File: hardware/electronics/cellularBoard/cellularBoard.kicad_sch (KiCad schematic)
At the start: 36 parts, among them J1 Standoff, J2 M.2_E_Key_PCB_Edge, U1 LM51571-Q1

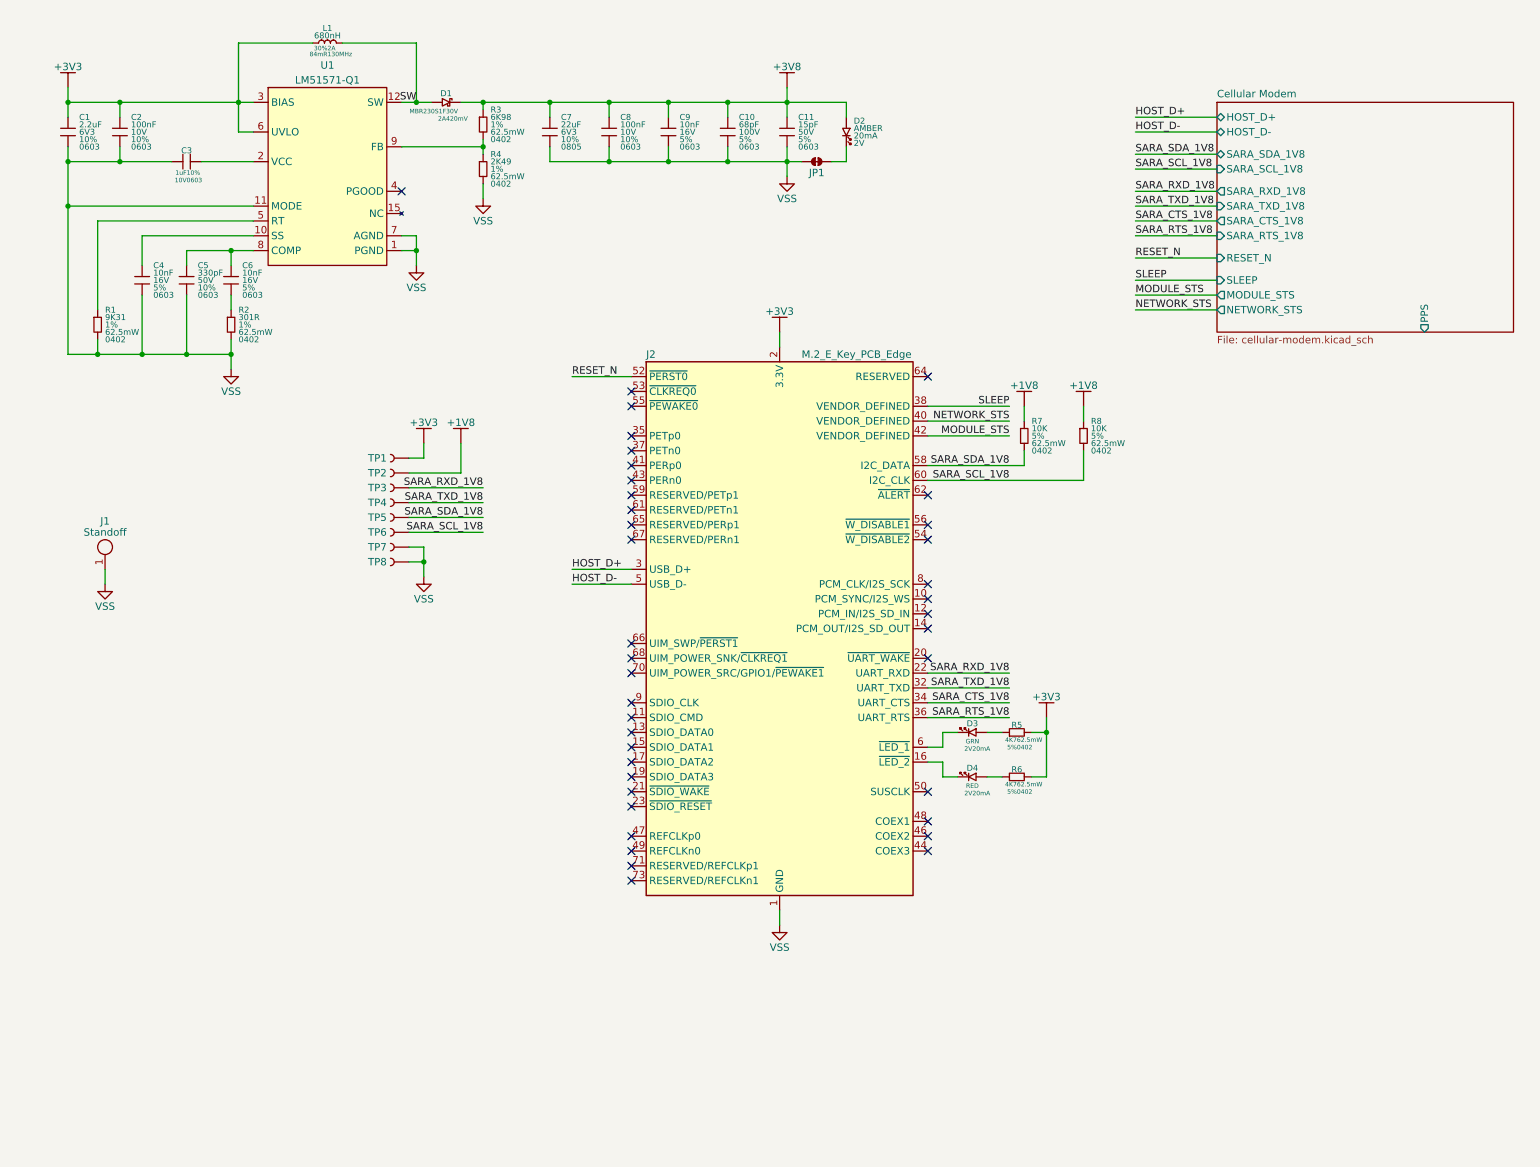
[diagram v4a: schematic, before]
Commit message: cleaned up schematic
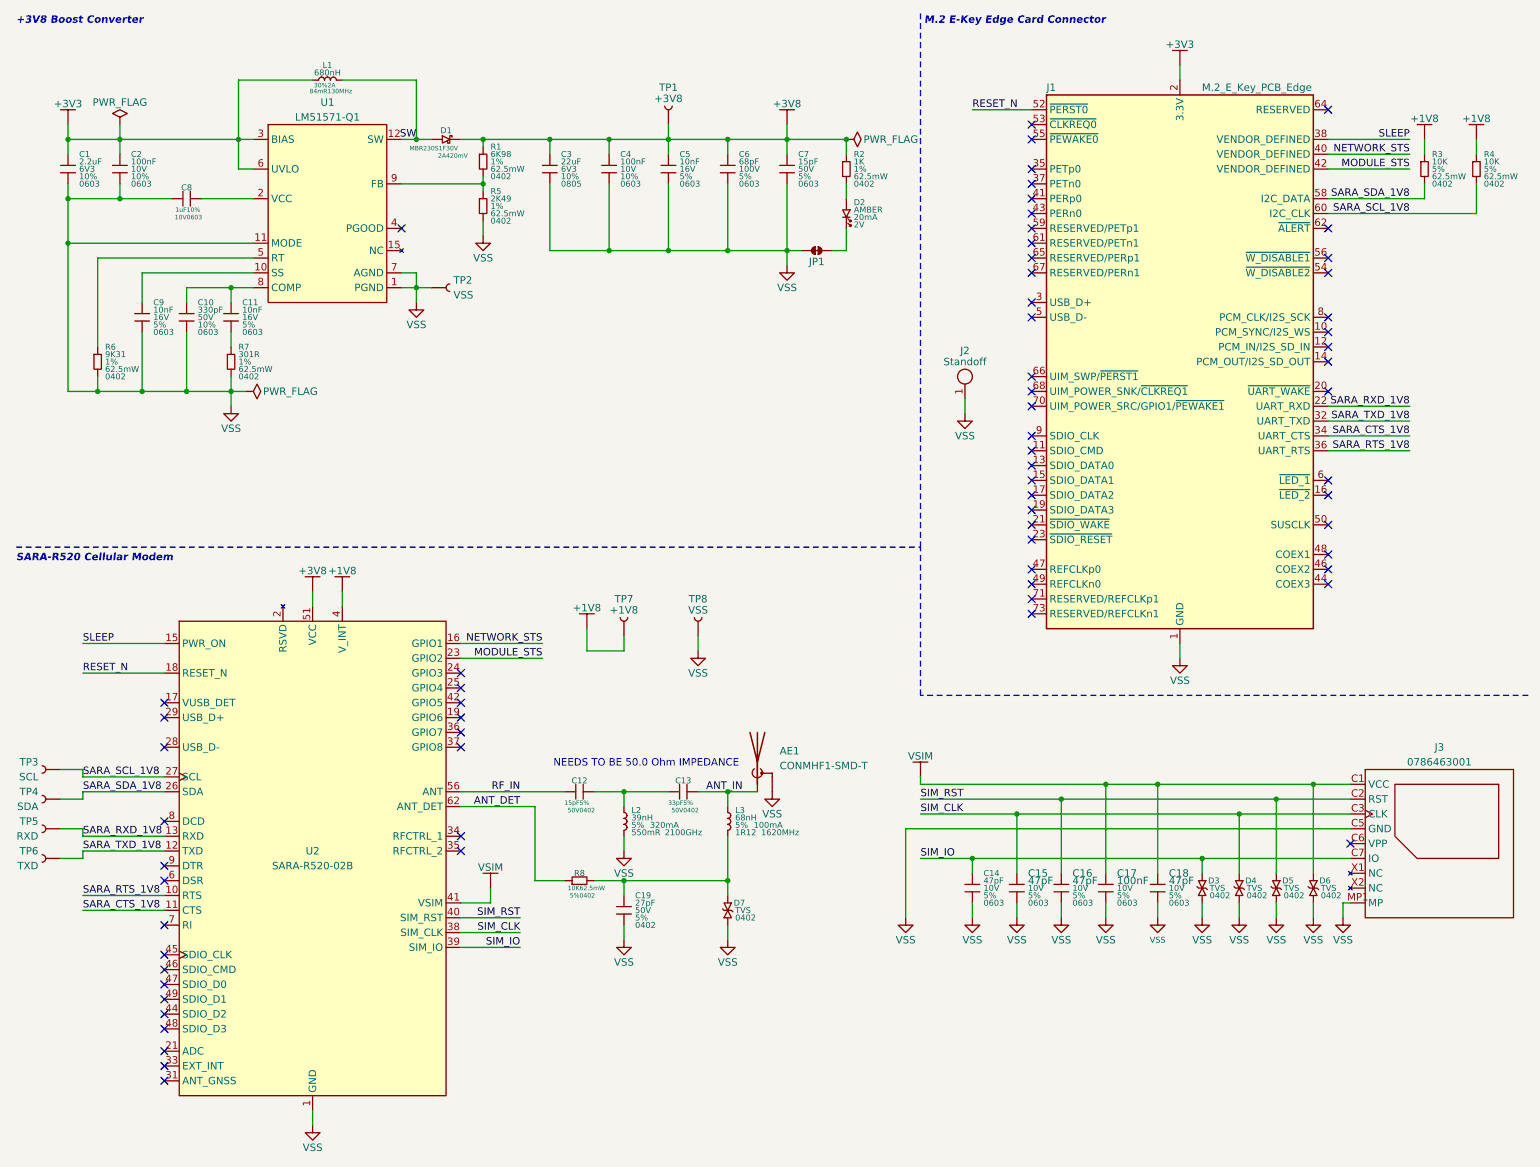
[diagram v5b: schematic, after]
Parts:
- removed D3: LTST-C190KGKT, lib_fp:LTST-0603, symbol lib_sch:LED_horizontal_1
- removed D4: LTST-C190KRKT, lib_fp:LTST-0603, symbol lib_sch:LED_horizontal_1
- removed R5, R6: 4K7, lib_fp:CRCW0402, symbol lib_sch:R_horizontal
- added AE1: CONMHF1-SMD-T, lib_fp:CONMHF1, symbol lib_sch:Antenna_Shield
- added C12: 15pF, lib_fp:MLCC0402, symbol lib_sch:C_horizontal
- added C13: 33pF, lib_fp:MLCC0402, symbol lib_sch:C_horizontal
- added C14, C15, C16, C18: 47pF, lib_fp:MLCC0603, symbol lib_sch:C
- added C17: 100nF, lib_fp:MLCC0603, symbol lib_sch:C
- added C19: 27pF, lib_fp:MLCC0402, symbol lib_sch:C
- added D3, D4, D5, D6, D7: TVS, lib_fp:XDFN2P65_100X60X50L50X25L, symbol lib_sch:D_TVS
- added J3: 0786463001, lib_fp:786463001, symbol lib_sch:SIM_Card
- added L2: 39nH, lib_fp:L_0402, symbol lib_sch:L
- added L3: 68nH, lib_fp:L_0402, symbol lib_sch:L
- added R2: 1K, lib_fp:CRCW0402, symbol lib_sch:R
- added R8: 10K, lib_fp:CRCW0402, symbol lib_sch:R_horizontal
- added U2: SARA-R520-02B, lib_fp:SARA-R52X_UBL, symbol lib_sch:SARA-R52
- TP1: value ~ -> +3V8
- TP2, TP8: value ~ -> VSS
- TP3: value ~ -> SCL
- TP4: value ~ -> SDA
- TP5: value ~ -> RXD
- TP6: value ~ -> TXD
- TP7: value ~ -> +1V8
- renumbered C5 to C10, C6 to C11, C7 to C3, C8 to C4, C9 to C5, C10 to C6, C11 to C7, C3 to C8, C4 to C9, J2 to J1, J1 to J2, R3 to R1, R7 to R3, R8 to R4, R4 to R5, R1 to R6, R2 to R7
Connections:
- net +1V8: now also TP7.1, U2.4 (V_INT); no longer TP2.1
- net +3V3: no longer TP1.1
- net +3V8: now also TP1.1, R2.1, U2.51 (VCC), U2.52 (VCC), U2.53 (VCC); no longer D2.1
- net MODULE_STS: now also U2.23 (GPIO2)
- net NETWORK_STS: now also U2.16 (GPIO1)
- net RESET_N: now also U2.18 (RESET_N)
- net SARA_CTS_1V8: now also U2.11 (CTS)
- net SARA_RTS_1V8: now also U2.10 (RTS)
- net SARA_RXD_1V8: now also TP5.1, U2.13 (RXD); no longer TP3.1
- net SARA_SCL_1V8: now also TP3.1, U2.27 (SCL); no longer TP6.1
- net SARA_SDA_1V8: now also TP4.1, U2.26 (SDA); no longer TP5.1
- net SARA_TXD_1V8: now also TP6.1, U2.12 (TXD); no longer TP4.1
- net SLEEP: now also U2.15 (PWR_ON)
- net VSS: now also TP2.1, AE1.2 (Shield), C14.2, C15.2, C16.2, C17.2, C18.2, C19.2, D3.1, D4.1, D5.1, D6.1, D7.1, J3.C5 (GND), J3.MP1 (MP), J3.MP2 (MP), J3.MP3 (MP), J3.MP4 (MP), J3.MP5 (MP), J3.MP6 (MP), L2.2, U2.1 (GND), U2.14 (GND), U2.20 (GND), U2.22 (GND), U2.3 (GND), U2.30 (GND), U2.32 (GND), U2.43 (GND), U2.5 (GND), U2.50 (GND), U2.54 (GND), U2.55 (GND), U2.57 (GND), U2.58 (GND), U2.59 (GND), U2.60 (GND), U2.61 (GND), U2.63 (GND), U2.64 (GND), U2.65 (GND), U2.66 (GND), U2.67 (GND), U2.68 (GND), U2.69 (GND), U2.70 (GND), U2.71 (GND), U2.72 (GND), U2.73 (GND), U2.74 (GND), U2.75 (GND), U2.76 (GND), U2.77 (GND), U2.78 (GND), U2.79 (GND), U2.80 (GND), U2.81 (GND), U2.82 (GND), U2.83 (GND), U2.84 (GND), U2.85 (GND), U2.86 (GND), U2.87 (GND), U2.88 (GND), U2.89 (GND), U2.90 (GND), U2.91 (GND), U2.92 (GND), U2.93 (GND), U2.94 (GND), U2.95 (GND), U2.96 (GND); no longer TP7.1
- net HOST_D+: no longer names the net of J1.3 (USB_D+)
- net HOST_D-: no longer names the net of J1.5 (USB_D-)
- new net: C12.2, C13.1, L2.1
- new net: C19.1, D7.2, L3.2, R8.2
- new net: D2.1, R2.2
- new net ANT_DET: R8.1, U2.62 (ANT_DET)
- new net ANT_IN: AE1.1 (A), C13.2, L3.1
- new net RF_IN: C12.1, U2.56 (ANT)
- new net SIM_CLK: C15.1, D4.2, J3.C3 (CLK), U2.38 (SIM_CLK)
- new net SIM_IO: C14.1, D3.2, J3.C7 (IO), U2.39 (SIM_IO)
- new net SIM_RST: C16.1, D5.2, J3.C2 (RST), U2.40 (SIM_RST)
- new net VSIM: C17.1, C18.1, D6.2, J3.C1 (VCC), U2.41 (VSIM)
- no-connect marks 39 -> 68
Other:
- removed sheet Cellular Modem
- note added: "+3V8 Boost Converter"
- note added: "M.2 E-Key Edge Card Connector"
- note added: "NEEDS TO BE 50.0 Ohm IMPEDANCE"
- note added: "SARA-R520 Cellular Modem"
- moved on the sheet: C1, C10, C11, C2, C3, C4, C5, C6, C7, C8, C9, D1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

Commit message: changed TPs to exempt from BOM
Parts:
- JP1: footprint lib_fp:Jumper_2_Bridged -> lib_fp:SolderJumper-2_P1.3mm_Bridged_Pad1.0x1.5mm
- TP1, TP2, TP3, TP4, TP5, TP6, TP7, TP8: now left out of the parts list
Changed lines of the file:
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@@
 	(title_block
 		(title "U-bolx ZED-F9P M.2 E-Key")
-		(date "2024-12-06")
+		(date "2024-12-23")
 		(rev "01")
 		(comment 2 "PROTOTYPE")
@@
 		(unit 1)
 		(exclude_from_sim no)
-		(in_bom yes)
+		(in_bom no)
 		(on_board yes)
 		(dnp no)
@@
 		(unit 1)
 		(exclude_from_sim no)
-		(in_bom yes)
+		(in_bom no)
 		(on_board yes)
 		(dnp no)
@@
 		(unit 1)
 		(exclude_from_sim no)
-		(in_bom yes)
+		(in_bom no)
 		(on_board yes)
 		(dnp no)
@@
 		(unit 1)
 		(exclude_from_sim no)
-		(in_bom yes)
+		(in_bom no)
 		(on_board yes)
 		(dnp no)
@@
 		(unit 1)
 		(exclude_from_sim no)
-		(in_bom yes)
+		(in_bom no)
 		(on_board yes)
 		(dnp no)
@@
 		(unit 1)
 		(exclude_from_sim no)
-		(in_bom yes)
+		(in_bom no)
 		(on_board yes)
 		(dnp no)
@@
 			)
 		)
-		(property "Footprint" "lib_fp:Jumper_2_Bridged"
+		(property "Footprint" "lib_fp:SolderJumper-2_P1.3mm_Bridged_Pad1.0x1.5mm"
 			(at 147.32 50.8 0)
 			(effects
@@
 		(unit 1)
 		(exclude_from_sim no)
-		(in_bom yes)
+		(in_bom no)
 		(on_board yes)
 		(dnp no)
@@
 		(unit 1)
 		(exclude_from_sim no)
-		(in_bom yes)
+		(in_bom no)
 		(on_board yes)
 		(dnp no)

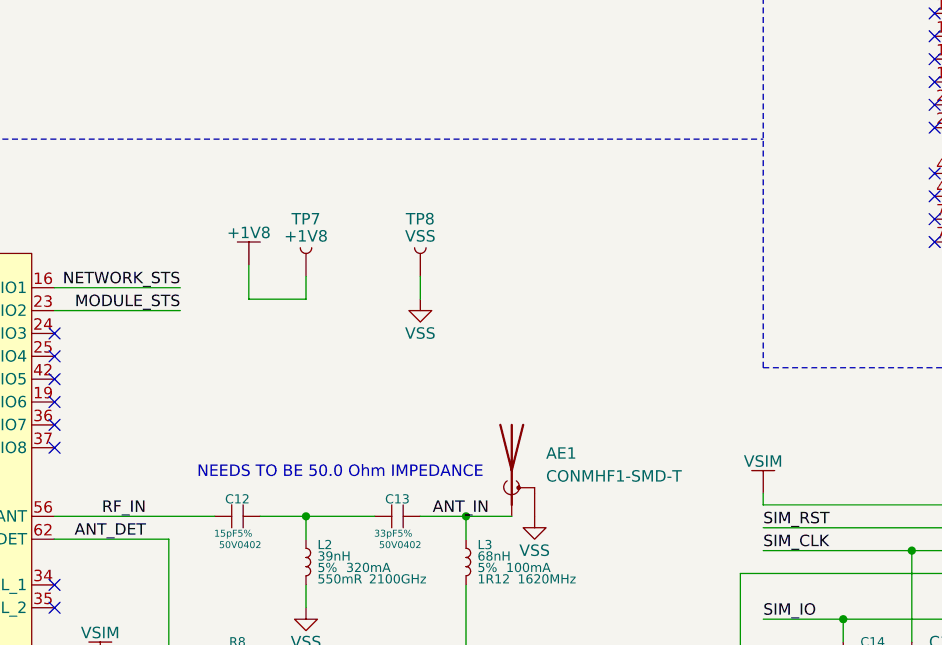
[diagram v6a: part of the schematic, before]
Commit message: added note for antenna feedline tracewidth
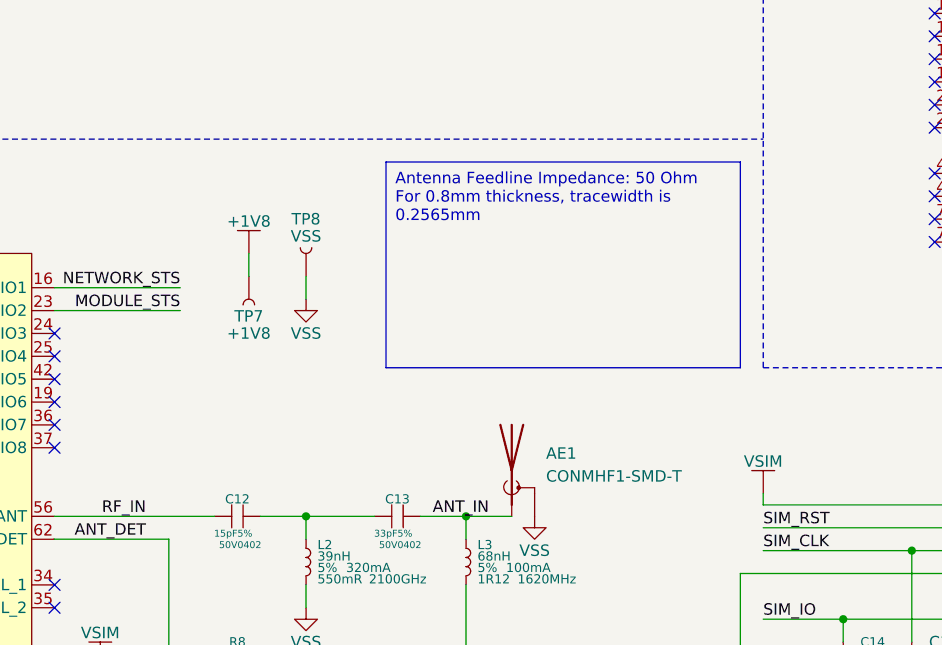
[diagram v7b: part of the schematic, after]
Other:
- note removed: "NEEDS TO BE 50.0 Ohm IMPEDANCE"
- moved on the sheet: TP7, TP8
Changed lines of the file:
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@@
 	(title_block
 		(title "U-bolx ZED-F9P M.2 E-Key")
-		(date "2024-12-23")
+		(date "2025-01-01")
 		(rev "01")
 		(comment 2 "PROTOTYPE")
-		(comment 3 "2024")
+		(comment 3 "2025")
 	)
 	(junction
@@
 	(wire
 		(pts
-			(xy 107.95 115.57) (xy 107.95 119.38)
-		)
-		(stroke
-			(width 0)
-			(type default)
-		)
-	)
-	(wire
-		(pts
 			(xy 181.61 147.32) (xy 219.71 147.32)
 		)
@@
 	(wire
 		(pts
-			(xy 107.95 119.38) (xy 114.3 119.38)
-		)
-		(stroke
-			(width 0)
-			(type default)
-		)
-	)
-	(wire
-		(pts
 			(xy 109.22 158.75) (xy 114.3 158.75)
 		)
@@
 	(wire
 		(pts
-			(xy 114.3 119.38) (xy 114.3 116.84)
+			(xy 107.95 114.3) (xy 107.95 116.84)
 		)
 		(stroke
@@
 	(wire
 		(pts
-			(xy 127 116.84) (xy 127 119.38)
+			(xy 114.3 116.84) (xy 114.3 119.38)
 		)
 		(stroke
@@
 		)
 	)
-	(text "NEEDS TO BE 50.0 Ohm IMPEDANCE"
+	(text_box "Antenna Feedline Impedance: 50 Ohm\nFor 0.8mm thickness, tracewidth is 0.2565mm"
 		(exclude_from_sim no)
-		(at 118.11 138.684 0)
+		(at 123.19 104.14 0)
+		(size 39.37 22.86)
+		(stroke
+			(width 0)
+			(type default)
+		)
+		(fill
+			(type none)
+		)
 		(effects
 			(font
 				(size 1.27 1.27)
 			)
+			(justify left top)
 		)
 	)
@@
 	(symbol
 		(lib_id "lib_sch:Testpoint")
-		(at 114.3 114.3 270)
+		(at 107.95 119.38 90)
 		(unit 1)
 		(exclude_from_sim no)
@@
 		(dnp no)
 		(property "Reference" "TP7"
-			(at 114.3 110.49 90)
+			(at 107.95 121.285 90)
 			(do_not_autoplace yes)
 			(effects
@@
 		)
 		(property "Value" "+1V8"
-			(at 114.3 112.395 90)
+			(at 107.95 123.19 90)
 			(do_not_autoplace yes)
 			(effects
@@
 		)
 		(property "Footprint" "lib_fp:TP_1mm"
-			(at 114.3 114.3 0)
+			(at 107.95 119.38 0)
 			(effects
 				(font
@@
 		)
 		(property "Datasheet" ""
-			(at 114.3 114.3 0)
+			(at 107.95 119.38 0)
 			(effects
 				(font
@@
 		)
 		(property "Description" ""
-			(at 114.3 114.3 0)
+			(at 107.95 119.38 0)
 			(effects
 				(font
@@
 		)
 		(property "Manufacturer" ""
-			(at 114.3 114.3 0)
+			(at 107.95 119.38 0)
 			(effects
 				(font
@@
 		)
 		(property "MPN" ""
-			(at 114.3 114.3 0)
+			(at 107.95 119.38 0)
 			(effects
 				(font
@@
 		)
 		(property "DKPN" ""
-			(at 114.3 114.3 0)
+			(at 107.95 119.38 0)
 			(effects
 				(font
@@
 	(symbol
 		(lib_id "lib_sch:Testpoint")
-		(at 127 114.3 270)
+		(at 114.3 114.3 270)
 		(unit 1)
 		(exclude_from_sim no)
@@
 		(dnp no)
 		(property "Reference" "TP8"
-			(at 127 110.49 90)
+			(at 114.3 110.49 90)
 			(do_not_autoplace yes)
 			(effects
@@
 		)
 		(property "Value" "VSS"
-			(at 127 112.395 90)
+			(at 114.3 112.395 90)
 			(do_not_autoplace yes)
 			(effects
@@
 		)
 		(property "Footprint" "lib_fp:TP_1mm"
-			(at 127 114.3 0)
+			(at 114.3 114.3 0)
 			(effects
 				(font
@@
 		)
 		(property "Datasheet" ""
-			(at 127 114.3 0)
+			(at 114.3 114.3 0)
 			(effects
 				(font
@@
 		)
 		(property "Description" ""
-			(at 127 114.3 0)
+			(at 114.3 114.3 0)
 			(effects
 				(font
@@
 		)
 		(property "Manufacturer" ""
-			(at 127 114.3 0)
+			(at 114.3 114.3 0)
 			(effects
 				(font
@@
 		)
 		(property "MPN" ""
-			(at 127 114.3 0)
+			(at 114.3 114.3 0)
 			(effects
 				(font
@@
 		)
 		(property "DKPN" ""
-			(at 127 114.3 0)
+			(at 114.3 114.3 0)
 			(effects
 				(font
@@
 	(symbol
 		(lib_id "lib_sch:VSS")
-		(at 127 119.38 0)
+		(at 114.3 119.38 0)
 		(unit 1)
 		(exclude_from_sim no)
@@
 		(fields_autoplaced yes)
 		(property "Reference" "#PWR010"
-			(at 127 119.38 0)
+			(at 114.3 119.38 0)
 			(effects
 				(font
@@
 		)
 		(property "Value" "VSS"
-			(at 127 123.19 0)
+			(at 114.3 123.19 0)
 			(do_not_autoplace yes)
 			(effects
@@
 		)
 		(property "Footprint" ""
-			(at 127 119.38 0)
+			(at 114.3 119.38 0)
 			(effects
 				(font
@@
 		)
 		(property "Datasheet" ""
-			(at 127 119.38 0)
+			(at 114.3 119.38 0)
 			(effects
 				(font
@@
 		)
 		(property "Description" ""
-			(at 127 119.38 0)
+			(at 114.3 119.38 0)
 			(effects
 				(font
@@
 	(symbol
 		(lib_id "lib_sch:+1V8")
-		(at 107.95 115.57 0)
+		(at 107.95 114.3 0)
 		(unit 1)
 		(exclude_from_sim no)
@@
 		(fields_autoplaced yes)
 		(property "Reference" "#PWR09"
-			(at 107.95 115.57 0)
+			(at 107.95 114.3 0)
 			(effects
 				(font
@@
 		)
 		(property "Value" "+1V8"
-			(at 107.95 112.014 0)
+			(at 107.95 110.744 0)
 			(do_not_autoplace yes)
 			(effects
@@
 		)
 		(property "Footprint" ""
-			(at 107.95 115.57 0)
+			(at 107.95 114.3 0)
 			(effects
 				(font
@@
 		)
 		(property "Datasheet" ""
-			(at 107.95 115.57 0)
+			(at 107.95 114.3 0)
 			(effects
 				(font
@@
 		)
 		(property "Description" ""
-			(at 107.95 115.57 0)
+			(at 107.95 114.3 0)
 			(effects
 				(font
